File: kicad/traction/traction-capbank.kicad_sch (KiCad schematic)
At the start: 26 parts

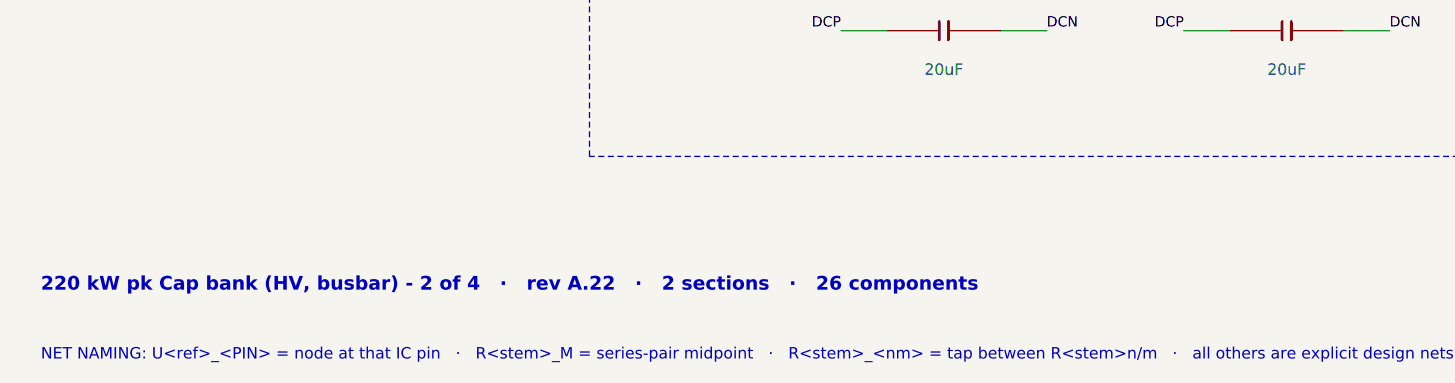
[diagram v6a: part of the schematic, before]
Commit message: Rev A.23: round 24 — four rechecks of 4ed0101 (F240–F244): the SDADC reference on its supply node, acquisition freshness, the map's flux slope and the ripple limiter's exact bounds, the temperature latch, the V_DC expiry
Hardware (F240, no new part): the S32K39 data sheet's SDADC table (Rev. 3 Table 38, in our archive and our own
extracted-parameters file) requires VREFP within ±25 mV of AVDD; the round-23 disposition had judged the general +100 mV
note and called the figure absent while the references sat on the FS26 VREF, matched to the SDADC-supply LDO only within
±1 %. Every non-R2R reference group (E6/H6 SAR, E10/F13 SDADC) is now on V5A itself with VDDA_SDADC and VDD_HV_A (NXP's
GEN3 arrangement); the ratiometric loads (HW_ID and offset dividers, the seven NTC pull-ups) moved with the reference; the
R2R ladder keeps the FS26 VREF as its isolated supply through the 10 Ω branch (CR2R1 330 nF, 37 kHz); CSB5 2.2 µF holds
the FS26 window alone (1.36–2.92 µF effective); the absolute SAR scale re-budgeted at the LDO2's ±1.75 %; ERC locks, pin
freeze, manifest, handoff §4.11 island rule (≤ 20 mΩ from E12 to any VREFH ball), VR-34 closed by design, IR-26, QP-TH-06.
Pipeline at A.23: ERC 981/0/0, verify 158/18/0, sim 23/6/0, Marine 87/23/0, 21 pages / 2065 pins, KiCad proof PASS, PDFs
and BOMs regenerated (₹72,983 unchanged). The handoff §6 gives every open pre-layout decision a provisional default.

Firmware (TI_FW_ID 0x0A0F0016, CAL layout 4, 191 fields / 92 CAL rows, 82 DTCs): F241 a stopped slow ADC channel stayed
valid forever (the caller discarded the acquisition stamp) → a three-state contract new/held/expired for every slow-list
input with cal_temp_hold_ms and DTC_ADC_SLOW_STALE, every slow consumer audited (V5GD/VOFS, IGN, INTRLOK_N, VSUP, HW_ID);
F242 the inductance map must keep a positive flux slope (≥ 0.25 × L0 below every breakpoint) and the ripple limiter bounds
every piece of its interval in closed form (breakpoints alone shown insufficient by a 20 000-m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
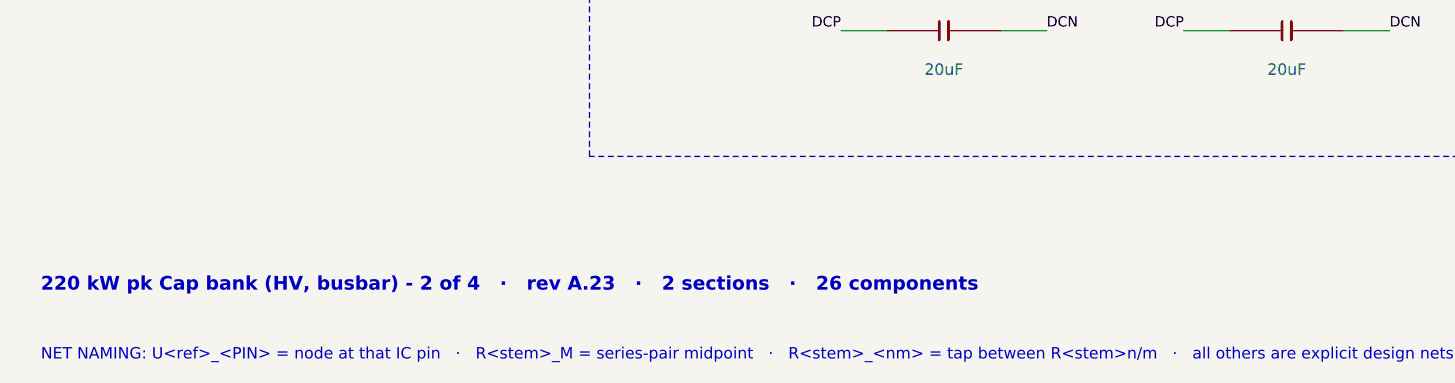
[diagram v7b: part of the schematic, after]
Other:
- note added: "220 kW pk Cap bank (HV, busbar) - 2 of 4 · rev A.23 · 2 sections · 26 components"
- note removed: "220 kW pk Cap bank (HV, busbar) - 2 of 4 · rev A.22 · 2 sections · 26 components"
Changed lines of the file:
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@@
 		(title "Traction Inverter — Cap bank (busbar assembly, 320 uF)")
 		(date "2026-09-23")
-		(rev "A.22")
+		(rev "A.23")
 		(company "Traction Inverter 220 kW pk - Cap bank (HV, busbar), sheet 2 of 4")
 		(comment 1 "Inverter = Power board + Cap bank busbar + bolt-on Discharge board (all HV) + Control card (LV); safe state holds with any link lost")
@@
 	(rectangle (start 12.7 12.7) (end 66.04 95.25) (stroke (width 0) (type dash)) (fill (type none)))
 	(rectangle (start 76.2 12.7) (end 193.04 114.3) (stroke (width 0) (type dash)) (fill (type none)))
-	(text "220 kW pk Cap bank (HV, busbar) - 2 of 4   ·   rev A.22   ·   2 sections   ·   26 components" (exclude_from_sim no) (at 15.24 129.54 0) (effects (font (size 1.524 1.524) (bold yes)) (justify left bottom)))
+	(text "220 kW pk Cap bank (HV, busbar) - 2 of 4   ·   rev A.23   ·   2 sections   ·   26 components" (exclude_from_sim no) (at 15.24 129.54 0) (effects (font (size 1.524 1.524) (bold yes)) (justify left bottom)))
 	(text "NET NAMING: U<ref>_<PIN> = node at that IC pin   ·   R<stem>_M = series-pair midpoint   ·   R<stem>_<nm> = tap between R<stem>n/m   ·   all others are explicit design nets   ·   same name on another sheet = same net, joined only at the named connector/stud/tab" (exclude_from_sim no) (at 15.24 137.16 0) (effects (font (size 1.27 1.27)) (justify left bottom)))
 	(text "CAP-BANK / BUS-STUDS" (exclude_from_sim no) (at 14.224 16.764 0) (effects (font (size 2.0066 2.0066) (bold yes)) (justify left bottom)))
